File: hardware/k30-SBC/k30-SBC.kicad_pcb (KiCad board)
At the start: 4 copper layers, 160 x 100 mm, 82 parts, among them J1 CompactFlash, J2 Serial1, J3 Serial2, J4 ADBUS-EXP, J5 ADBUS, J6 SIGBUS, J7 POWER, J8 POWER, J9 POWER, SW1 RESET, SW2 SW_DIP_x06, SW3 IP2, SW4 IP3, U1 MC68030FE, U10 74HC253, U11 74HC138, U12 74HC393, U13 MC68681, U14 AS6C8016, U15 AS6C8016, U16 AM29F040, U2 74HC14, U3 74HC05, U4 74HC139, U5 4072, U6 74HC20, U7 74HC32, U8 74HC08, U9 74HC253, Y1 Crystal, Y2 Crystal

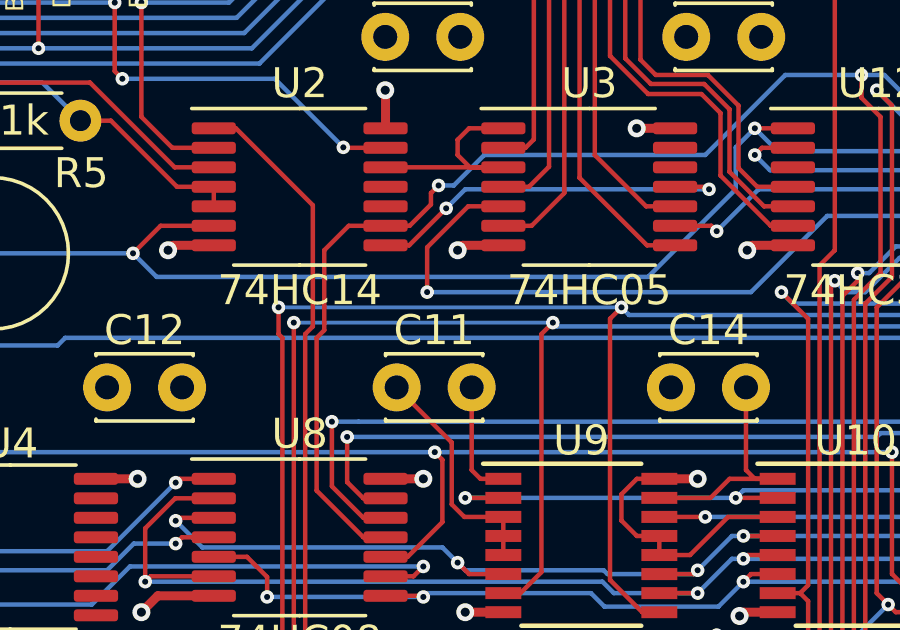
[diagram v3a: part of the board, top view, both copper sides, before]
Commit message: Final fixes to remove narrow traces
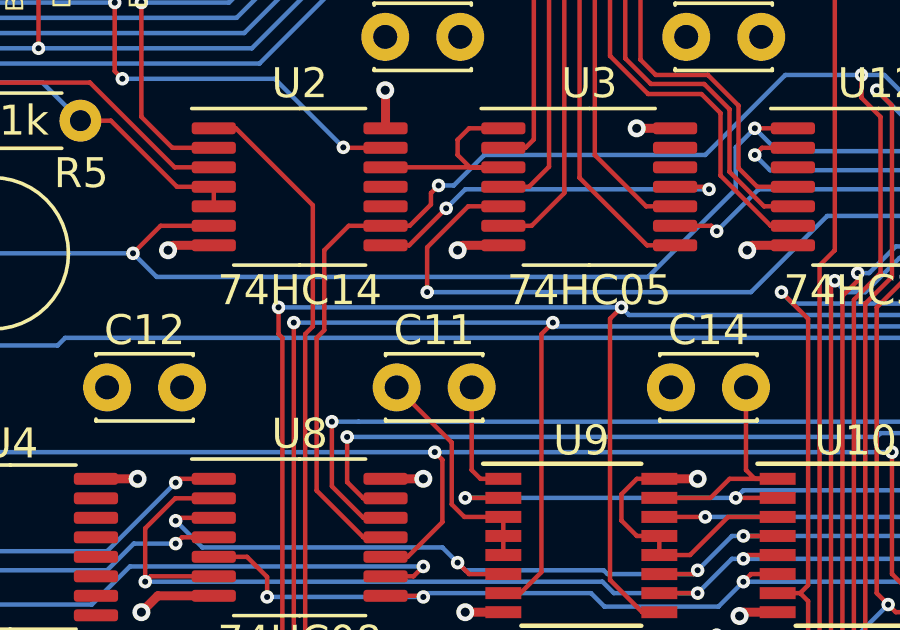
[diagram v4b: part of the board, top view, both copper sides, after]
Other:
- net class Narrow removed
- rule trace_min: 0.127 -> 0.15
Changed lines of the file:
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@@
   (setup
     (last_trace_width 0.15)
-    (user_trace_width 0.127)
     (user_trace_width 0.3)
     (user_trace_width 1)
@@
     (zone_clearance 0.508)
     (zone_45_only no)
-    (trace_min 0.127)
+    (trace_min 0.15)
     (via_size 0.45)
     (via_drill 0.2)
@@
     (add_net ~DS3)
   )
-  (net_class Narrow ""
-    (clearance 0.127)
-    (trace_width 0.127)
-    (via_dia 0.45)
-    (via_drill 0.2)
-    (uvia_dia 0.3)
-    (uvia_drill 0.1)
-  )
   (module Symbol:OSHW-Symbol_6.7x6mm_SilkScreen (layer F.Cu)
     (at 129.032 88.392)
@@
   (segment (start 137.287 63.246) (end 137.287 63.246) (width 0.15) (layer B.Cu) (net 62))
   (via (at 137.287 63.246) (size 0.45) (drill 0.2) (layers F.Cu B.Cu) (net 62))
-  (segment (start 137.287 63.246) (end 128.651 63.246) (width 0.127) (layer B.Cu) (net 62))
-  (segment (start 128.651 63.246) (end 128.651 63.246) (width 0.127) (layer B.Cu) (net 62))
-  (via (at 128.651 63.246) (size 0.45) (drill 0.2) (layers F.Cu B.Cu) (net 62))
+  (segment (start 137.287 63.246) (end 128.651 63.246) (width 0.15) (layer B.Cu) (net 62))
   (segment (start 126.237 104.637) (end 125.4745 104.637) (width 0.15) (layer F.Cu) (net 62))
   (segment (start 125.095 104.2575) (end 125.095 78.613) (width 0.15) (layer F.Cu) (net 62))
@@
   (segment (start 193.04 76.2) (end 190.881 76.2) (width 0.15) (layer B.Cu) (net 62))
   (segment (start 194.31 74.93) (end 193.04 76.2) (width 0.15) (layer B.Cu) (net 62))
+  (segment (start 128.651 63.246) (end 128.651 63.246) (width 0.15) (layer F.Cu) (net 62))
+  (via (at 128.651 63.246) (size 0.45) (drill 0.2) (layers F.Cu B.Cu) (net 62))
   (segment (start 139.573 62.738) (end 139.573 62.738) (width 0.15) (layer F.Cu) (net 63))
   (via (at 139.573 62.738) (size 0.45) (drill 0.2) (layers F.Cu B.Cu) (net 63))
@@
   (segment (start 139.192 71.824002) (end 139.192 63.119) (width 0.15) (layer F.Cu) (net 63))
   (segment (start 140.836 72.898) (end 140.265998 72.898) (width 0.15) (layer F.Cu) (net 63))
-  (segment (start 139.573 62.738) (end 128.143 62.738) (width 0.127) (layer B.Cu) (net 63))
-  (segment (start 128.143 62.738) (end 128.143 62.738) (width 0.127) (layer B.Cu) (net 63))
-  (via (at 128.143 62.738) (size 0.45) (drill 0.2) (layers F.Cu B.Cu) (net 63))
+  (segment (start 139.573 62.738) (end 128.143 62.738) (width 0.15) (layer B.Cu) (net 63))
   (segment (start 128.27 63.754) (end 128.143 63.627) (width 0.15) (layer F.Cu) (net 63))
   (segment (start 128.27 74.93) (end 128.27 63.754) (width 0.15) (layer F.Cu) (net 63))
@@
   (segment (start 126.237 105.437) (end 125.4745 105.437) (width 0.15) (layer F.Cu) (net 63))
   (segment (start 128.143 63.627) (end 128.143 62.738) (width 0.15) (layer F.Cu) (net 63))
+  (segment (start 128.143 62.738) (end 128.143 62.738) (width 0.15) (layer F.Cu) (net 63))
+  (via (at 128.143 62.738) (size 0.45) (drill 0.2) (layers F.Cu B.Cu) (net 63))
   (segment (start 145.288 62.611) (end 144.907 62.23) (width 0.15) (layer B.Cu) (net 64))
   (segment (start 151.257 62.611) (end 145.288 62.611) (width 0.15) (layer B.Cu) (net 64))
